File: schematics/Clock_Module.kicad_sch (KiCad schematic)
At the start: 28 parts, among them SW1 SW_SPDT, SW2 SW_Push, U1 LM555CN, U3 LM555CN, U4 74LS08, U5 74LS32, U6 74LS04, U7 LM555CN

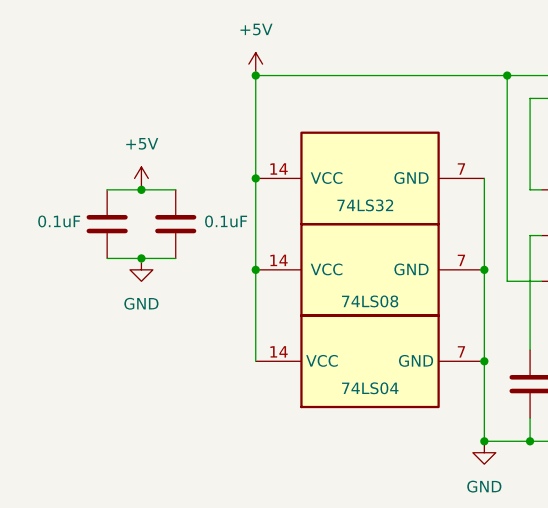
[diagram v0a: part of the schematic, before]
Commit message: feat: updated electrical diagrams & individual part list
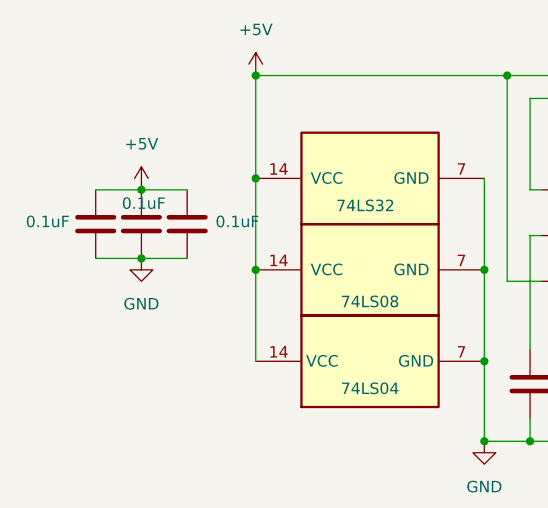
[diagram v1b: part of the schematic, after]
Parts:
- added C8: 0.1uF, symbol Device:C
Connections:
- net +5V: now also C8.2
- net GND: now also C8.1
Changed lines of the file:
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@@
 	(wire
 		(pts
-			(xy 24.13 111.76) (xy 27.94 111.76)
+			(xy 24.13 111.76) (xy 29.21 111.76)
 		)
 		(stroke
@@
 	(wire
 		(pts
-			(xy 24.13 104.14) (xy 27.94 104.14)
+			(xy 24.13 104.14) (xy 29.21 104.14)
 		)
 		(stroke
@@
 	(wire
 		(pts
-			(xy 24.13 111.76) (xy 20.32 111.76)
+			(xy 24.13 111.76) (xy 19.05 111.76)
 		)
 		(stroke
@@
 	(wire
 		(pts
-			(xy 20.32 104.14) (xy 24.13 104.14)
+			(xy 19.05 104.14) (xy 24.13 104.14)
 		)
 		(stroke
@@
 	(symbol
 		(lib_id "Device:C")
-		(at 27.94 107.95 180)
+		(at 24.13 107.95 180)
+		(unit 1)
+		(exclude_from_sim no)
+		(in_bom yes)
+		(on_board yes)
+		(dnp no)
+		(property "Reference" "C8"
+			(at 22.352 104.394 90)
+			(effects
+				(font
+					(size 1.27 1.27)
+				)
+				(hide yes)
+			)
+		)
+		(property "Value" "0.1uF"
+			(at 24.384 105.664 0)
+			(effects
+				(font
+					(size 1.27 1.27)
+				)
+			)
+		)
+		(property "Footprint" ""
+			(at 23.1648 104.14 0)
+			(effects
+				(font
+					(size 1.27 1.27)
+				)
+				(hide yes)
+			)
+		)
+		(property "Datasheet" "~"
+			(at 24.13 107.95 0)
+			(effects
+				(font
+					(size 1.27 1.27)
+				)
+				(hide yes)
+			)
+		)
+		(property "Description" "Unpolarized capacitor"
+			(at 24.13 107.95 0)
+			(effects
+				(font
+					(size 1.27 1.27)
+				)
+				(hide yes)
+			)
+		)
+		(pin "2"
+		)
+		(pin "1"
+		)
+		(instances
+			(project "Clock_Module"
+				(path "/00881835-431f-440c-8b02-f05a8dfd3447"
+					(reference "C8")
+					(unit 1)
+				)
+			)
+		)
+	)
+	(symbol
+		(lib_id "Device:C")
+		(at 29.21 107.95 180)
 		(unit 1)
 		(exclude_from_sim no)
@@
 		(dnp no)
 		(property "Reference" "C6"
-			(at 26.162 104.394 90)
+			(at 27.432 104.394 90)
 			(effects
 				(font
@@
 		)
 		(property "Value" "0.1uF"
-			(at 33.528 107.696 0)
+			(at 34.798 107.696 0)
 			(effects
 				(font
@@
 		)
 		(property "Footprint" ""
-			(at 26.9748 104.14 0)
+			(at 28.2448 104.14 0)
 			(effects
 				(font
@@
 		)
 		(property "Datasheet" "~"
-			(at 27.94 107.95 0)
+			(at 29.21 107.95 0)
 			(effects
 				(font
@@
 		)
 		(property "Description" "Unpolarized capacitor"
-			(at 27.94 107.95 0)
+			(at 29.21 107.95 0)
 			(effects
 				(font
@@
 	(symbol
 		(lib_id "Device:C")
-		(at 20.32 107.95 180)
+		(at 19.05 107.95 180)
 		(unit 1)
 		(exclude_from_sim no)
@@
 		(dnp no)
 		(property "Reference" "C5"
-			(at 18.542 104.394 90)
+			(at 17.272 104.394 90)
 			(effects
 				(font
@@
 		)
 		(property "Value" "0.1uF"
-			(at 14.986 107.696 0)
+			(at 13.716 107.696 0)
 			(effects
 				(font
@@
 		)
 		(property "Footprint" ""
-			(at 19.3548 104.14 0)
+			(at 18.0848 104.14 0)
 			(effects
 				(font
@@
 		)
 		(property "Datasheet" "~"
-			(at 20.32 107.95 0)
+			(at 19.05 107.95 0)
 			(effects
 				(font
@@
 		)
 		(property "Description" "Unpolarized capacitor"
-			(at 20.32 107.95 0)
+			(at 19.05 107.95 0)
 			(effects
 				(font

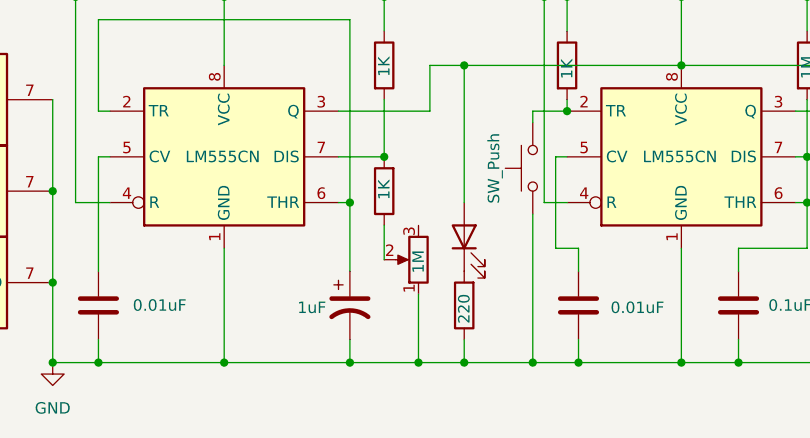
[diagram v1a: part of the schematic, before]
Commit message: Updated schematics and README
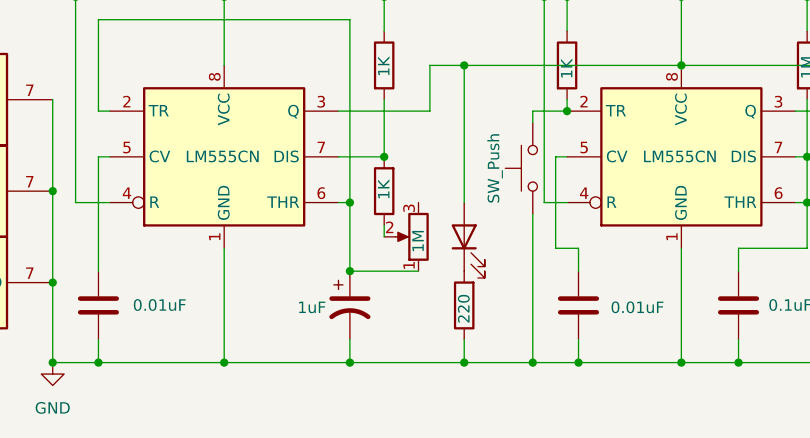
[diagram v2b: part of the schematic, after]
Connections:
- net GND: no longer 1M.1
- net at C7.1, U1.2 (TR), U1.6 (THR): now also 1M.1
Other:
- moved on the sheet: 1M
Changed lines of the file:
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@@
+	)
+	(junction
+		(at 95.25 121.92)
+		(diameter 0)
+		(color 0 0 0 0)
 	)
 	(junction
@@
 	)
 	(junction
-		(at 102.87 132.08)
-		(diameter 0)
-		(color 0 0 0 0)
-	)
-	(junction
 		(at 119.38 104.14)
 		(diameter 0)
@@
 	(wire
 		(pts
-			(xy 99.06 116.84) (xy 99.06 120.65)
+			(xy 99.06 116.84) (xy 99.06 118.11)
 		)
 		(stroke
@@
 	(wire
 		(pts
+			(xy 95.25 121.92) (xy 102.87 121.92)
+		)
+		(stroke
+			(width 0)
+			(type default)
+		)
+	)
+	(wire
+		(pts
 			(xy 273.05 106.68) (xy 271.78 106.68)
 		)
@@
 	(wire
 		(pts
-			(xy 95.25 132.08) (xy 102.87 132.08)
+			(xy 95.25 132.08) (xy 107.95 132.08)
 		)
 		(stroke
@@
 	(wire
 		(pts
-			(xy 102.87 124.46) (xy 102.87 132.08)
-		)
-		(stroke
-			(width 0)
-			(type default)
-		)
-	)
-	(wire
-		(pts
 			(xy 224.79 102.87) (xy 224.79 106.68)
 		)
@@
 		(pts
 			(xy 67.31 93.98) (xy 95.25 93.98)
-		)
-		(stroke
-			(width 0)
-			(type default)
-		)
-	)
-	(wire
-		(pts
-			(xy 102.87 132.08) (xy 107.95 132.08)
 		)
 		(stroke
@@
 	(symbol
 		(lib_id "Device:R_Potentiometer")
-		(at 102.87 120.65 180)
+		(at 102.87 118.11 180)
 		(unit 1)
 		(exclude_from_sim no)
@@
 		(dnp no)
 		(property "Reference" "1M"
-			(at 102.87 122.174 90)
+			(at 102.87 119.888 90)
 			(effects
 				(font
@@
 		)
 		(property "Value" "R_Potentiometer"
-			(at 105.41 121.9199 0)
+			(at 105.41 119.3799 0)
 			(effects
 				(font
@@
 		)
 		(property "Footprint" ""
-			(at 102.87 120.65 0)
+			(at 102.87 118.11 0)
 			(effects
 				(font
@@
 		)
 		(property "Datasheet" "~"
-			(at 102.87 120.65 0)
+			(at 102.87 118.11 0)
 			(effects
 				(font
@@
 		)
 		(property "Description" "Potentiometer"
-			(at 102.87 120.65 0)
-			(effects
-				(font
+			(at 102.87 118.11 0)
+			(effects
+				(font
